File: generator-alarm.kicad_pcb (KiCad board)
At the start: 2 copper layers, 26 x 36 mm, 25 parts, among them J1 Sensor, J2 UART, J3 SWD, J4 12V, SW1 RESET, U1 RA-02, U2 STM32F030K6Tx, U3 XC6206P332PR-G

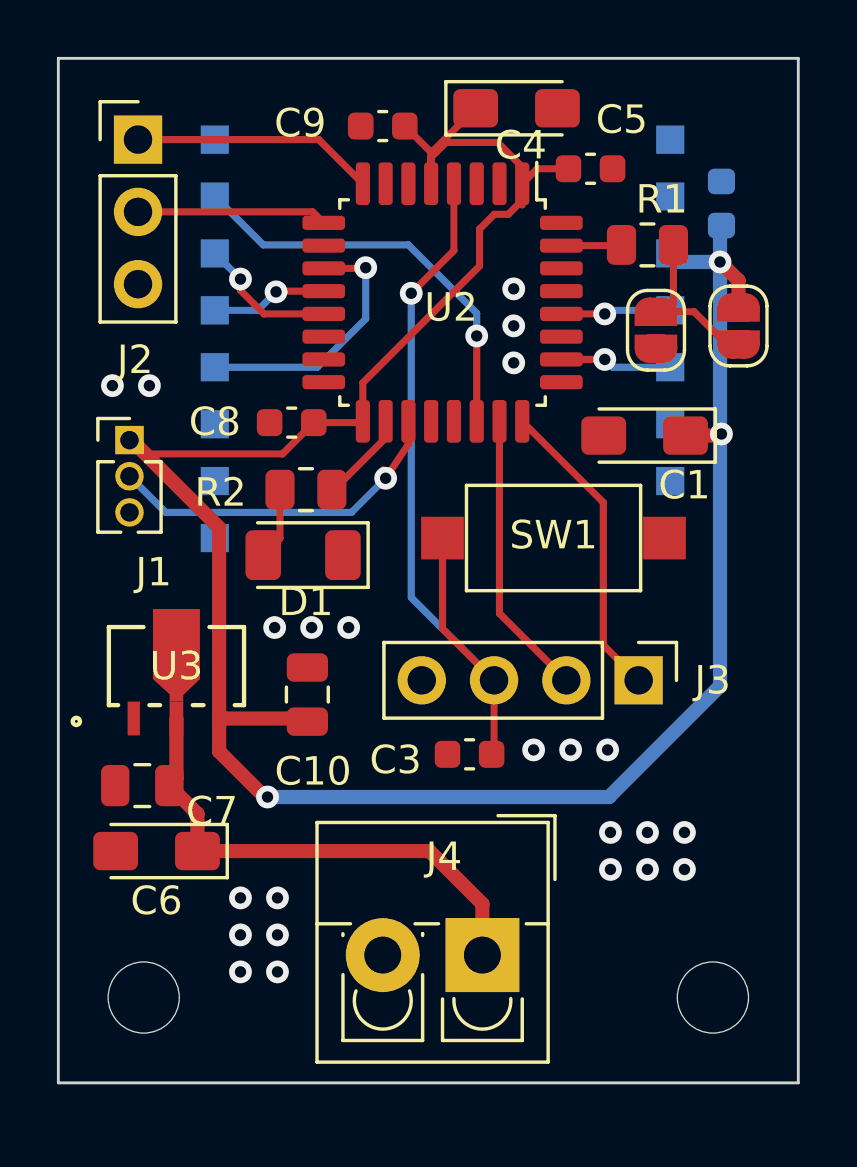
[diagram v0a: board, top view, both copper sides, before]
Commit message: Add USB-C connector and Li-Ion charger controller
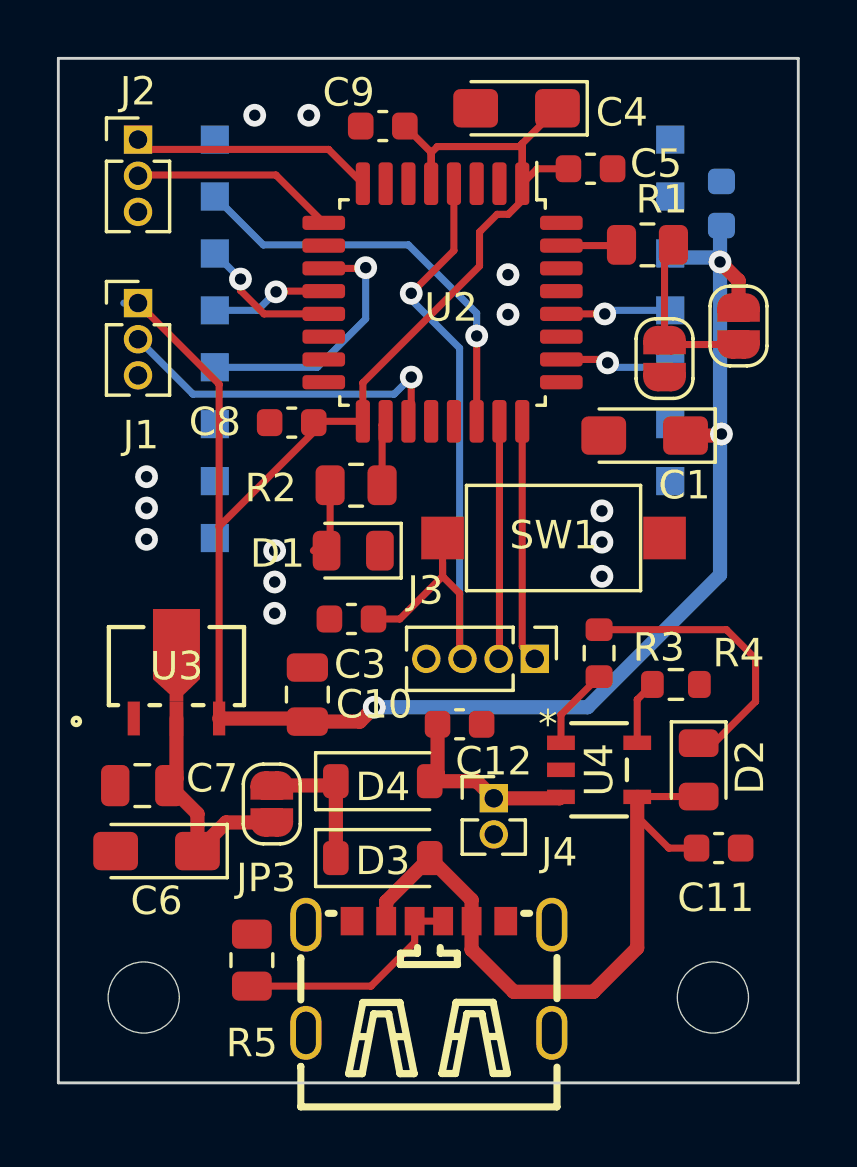
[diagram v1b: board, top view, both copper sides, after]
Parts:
- added C11: 1u, Capacitor_SMD:C_0603_1608Metric, F.Cu at (23.2, 27.8)
- added C12: 10u, Capacitor_SMD:C_0603_1608Metric, F.Cu at (14.1, 23.4)
- added D2: LED-Blue, LED_SMD:LED_0805_2012Metric, F.Cu at (22.5, 25.0)
- added D3: MBR0520LT1, Diode_SMD:D_SOD-123, F.Cu at (11.4, 28.1)
- added D4: MBR0520LT1, Diode_SMD:D_SOD-123, F.Cu at (11.4, 25.4)
- added JP3: SolderJumper_2_Open, Jumper:SolderJumper-2_P1.3mm_Open_RoundedPad1.0x1.5mm, F.Cu at (7.50, 26.2)
- added R3: 3k, Resistor_SMD:R_0603_1608Metric, F.Cu at (19.0, 20.9)
- added R4: 5k, Resistor_SMD:R_0603_1608Metric, F.Cu at (21.7, 22.0)
- added R5: 5.1k, Resistor_SMD:R_0805_2012Metric, F.Cu at (6.80, 31.7)
- added U4: TP4065-4.2V-SOT25-R, footprints2:SOT-23-5L_TPW, F.Cu at (19.0, 25.0)
- added USB1: TYPE-C_6P, kicad_lceda:TYPE-C-SMD_TYPE-C-6P, F.Cu at (13.0, 32.3)
- D1: footprint LED_SMD:LED_1206_3216Metric -> LED_SMD:LED_0805_2012Metric
- J2: footprint Connector_PinHeader_2.54mm:PinHeader_1x03_P2.54mm_Vertical -> Connector_PinHeader_1.27mm:PinHeader_1x03_P1.27mm_Vertical
- J3: footprint Connector_PinHeader_2.54mm:PinHeader_1x04_P2.54mm_Vertical -> Connector_PinHeader_1.27mm:PinHeader_1x04_P1.27mm_Vertical
- J4: value 12V -> BAT; footprint TerminalBlock_4Ucon:TerminalBlock_4Ucon_1x02_P3.50mm_Vertical -> Connector_PinHeader_1.27mm:PinHeader_1x02_P1.27mm_Vertical
- moved C3 6.31 mm to (10.3, 19.7)
- moved J4 5.52 mm to (15.3, 26.0), turned to 0 degrees
- moved J1 4.82 mm to (2.80, 8.60)
- moved J3 3.73 mm to (16.7, 21.1)
- moved D1 1.77 mm to (10.4, 17.3)
- moved R2 1.77 mm to (10.5, 15.0)
- moved JP1 1.04 mm to (21.3, 10.6)
- turned C4 to 180 degrees
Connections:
- net GND renamed BAT-
- C6 pad 1: Net-(J4-Pin_1) -> V+
- C7 pad 1: Net-(J4-Pin_1) -> V+
- J4 pad 1: Net-(J4-Pin_1) -> BAT+
- U3 pad 2: Net-(J4-Pin_1) -> V+
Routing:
- net Net-(D2-A): track 0.00 -> 24.3 mm
- net Net-(J4-Pin_1): track 17.8 -> 0.00 mm
- net Net-(D2-K): track 0.00 -> 10.0 mm
- net V+: track 0.00 -> 8.20 mm
- net Net-(USB1-CC1): track 0.00 -> 8.10 mm
- net BAT+: track 0.00 -> 6.99 mm
- net VDD: track 90.7 -> 84.4 mm
- net Net-(D3-K): track 0.00 -> 5.01 mm
- net Net-(U4-CHRG): track 0.00 -> 2.88 mm
- net Net-(U4-PROG): track 0.00 -> 2.27 mm
- net SWCLK: track 10.8 -> 8.53 mm
- net NRST: track 28.3 -> 26.1 mm
- net SWDIO: track 10.1 -> 8.36 mm
- net Net-(U2-PA8): track 3.23 -> 2.30 mm
- net UART_RX: track 6.68 -> 7.23 mm
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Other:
- board text added: "ARS v1.1"
- board text removed: "ARS v1.0"
